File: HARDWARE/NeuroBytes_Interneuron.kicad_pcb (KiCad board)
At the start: 2 copper layers, 58.4 x 25.1 mm, 31 parts, among them P1 JST GH 4-POS, P2 JST GH 4-POS, P3 JST GH 4-POS, P4 JST GH 4-POS, P5 JST GH 4-POS, P6 JST GH 4-POS, P7 JST GH 4-POS, P8 JST_GH_5-pos, Q1 MMBT3904, Q2 MMBT3904, Q3 MMBT3904, SW1 SW_PUSH_TL3330AF130QG, U1 STM32L011Gx, U2 TLV702

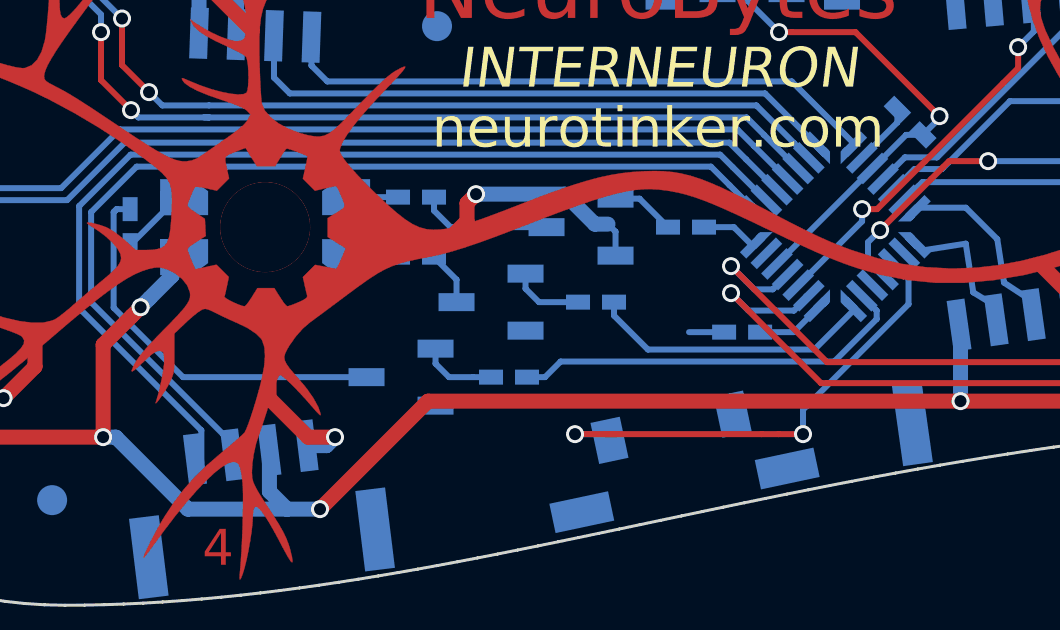
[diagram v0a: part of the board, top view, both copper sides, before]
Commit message: added ESD protection. updated title block.
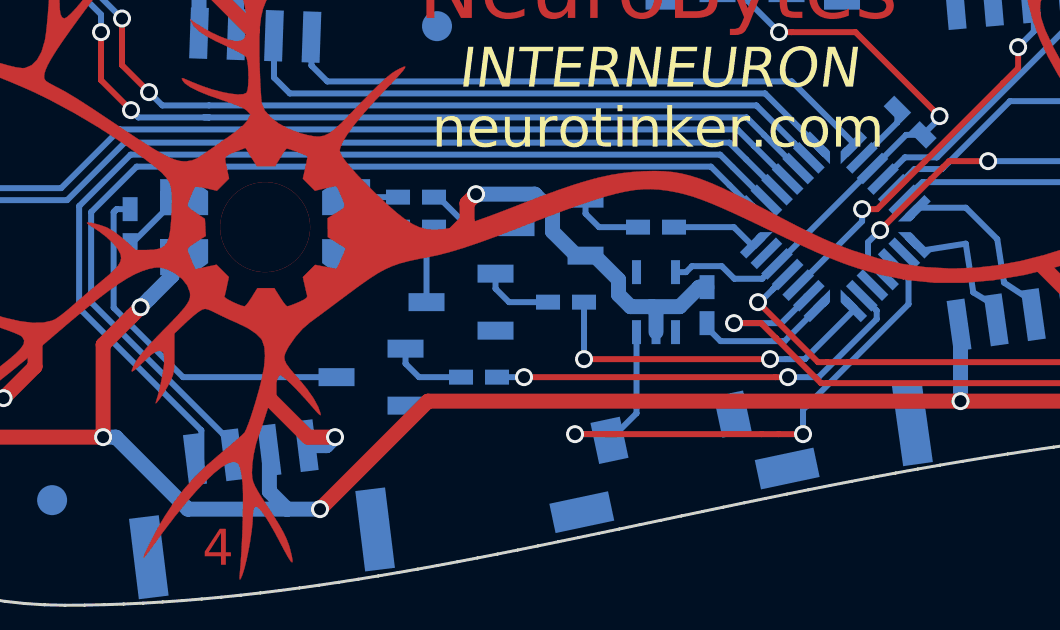
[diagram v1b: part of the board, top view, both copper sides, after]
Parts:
- added U3: RClamp0503F, KiCad_Footprints:ZF_SMD_SOT-353, B.Cu at (163.0, 92.5)
- moved R4 1.48 mm to (164.7, 92.6), turned to 90 degrees
- moved Q1 1.00 mm to (156.5, 92.5)
- moved Q2 1.00 mm to (159.5, 90.0)
- moved Q3 1.00 mm to (153.5, 95.0)
- moved R1 1.00 mm to (155.0, 90.0)
- moved R5 1.00 mm to (160.0, 92.5)
- moved R6 1.00 mm to (163.0, 90.0)
- moved R7 1.00 mm to (157.1, 95.0)
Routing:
- net SWITCH: track 16.3 -> 20.3 mm
- net GND: track 51.1 -> 55.1 mm
- net +3V3: track 22.8 -> 26.6 mm
- net LED_R: track 9.49 -> 11.7 mm, vias 0 -> 2
- net Net-(R4-Pad1): track 2.87 -> 4.71 mm
- net RESET: track 21.4 -> 19.7 mm
- net Net-(Q2-Pad3): track 4.43 -> 3.16 mm
- net Net-(Q3-Pad3): track 13.3 -> 12.3 mm
- net LED_B: track 13.4 -> 14.4 mm, vias 0 -> 2
- net LED_G: track 1.88 -> 2.68 mm
- net Net-(Q1-Pad3): track 1.81 -> 2.60 mm
- net A3EX: track 24.9 -> 24.2 mm

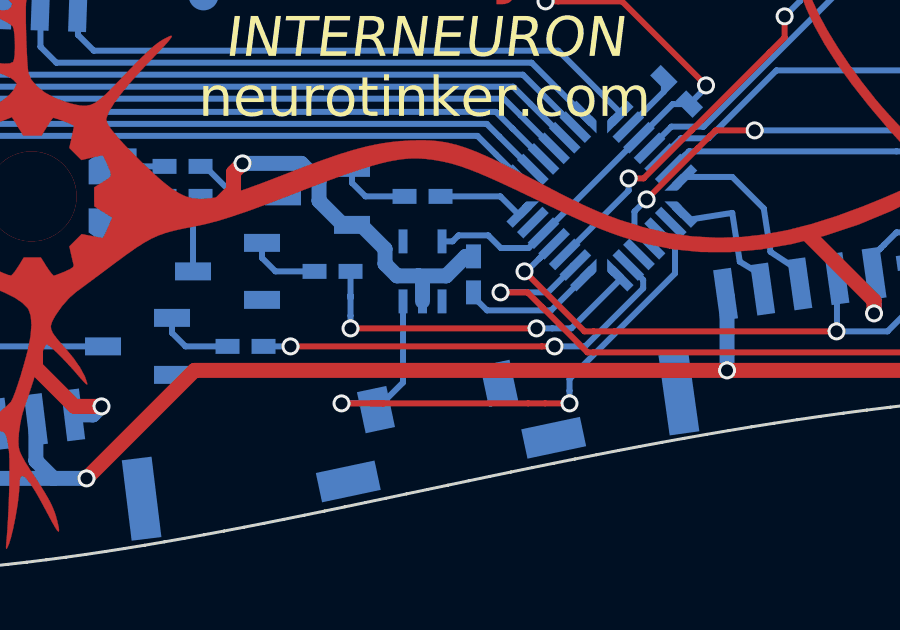
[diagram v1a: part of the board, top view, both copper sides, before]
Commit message: removed ESD protection (not needed during testing). generated fab files and BOM.
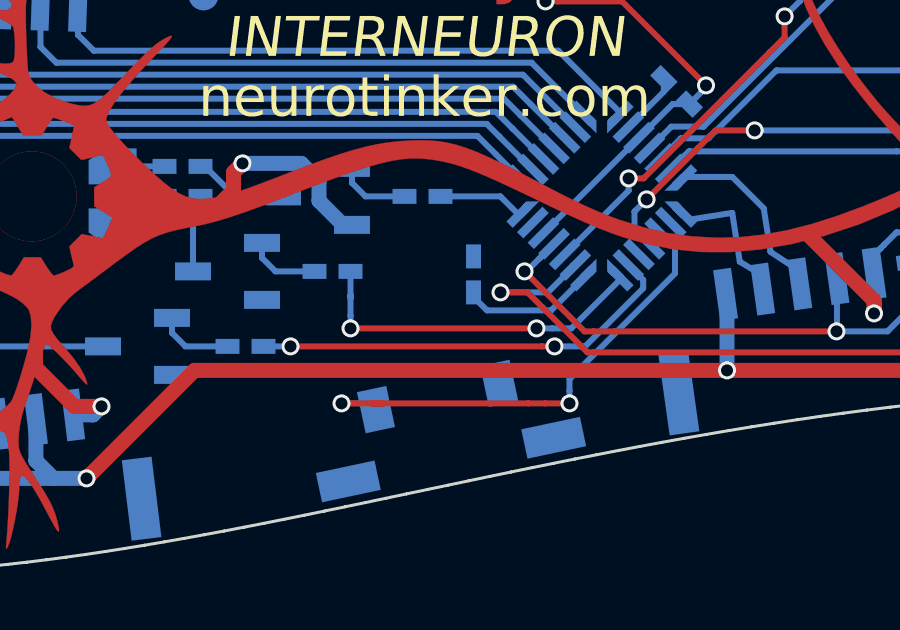
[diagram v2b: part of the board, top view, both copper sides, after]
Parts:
- removed U3: RClamp0503F, KiCad_Footprints:ZF_SMD_SOT-353
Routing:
- net GND: track 55.1 -> 49.2 mm
- net SWITCH: track 20.3 -> 16.3 mm
- net +3V3: track 26.6 -> 22.8 mm
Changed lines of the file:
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@@
     (links 104)
     (no_connects 0)
-    (area 130.957187 77.474012 189.496654 102.653506)
+    (area 123.4 55.4 221.257146 138.425)
     (thickness 1.6)
     (drawings 257)
-    (tracks 444)
+    (tracks 427)
     (zones 0)
-    (modules 32)
-    (nets 41)
+    (modules 31)
+    (nets 39)
   )
   (page A)
@@
       (drillshape 0)
       (scaleselection 1)
-      (outputdirectory ../../../NeuroTinker_RFQ_Sept2017/NeuroBytes_Interneuron/))
+      (outputdirectory ""))
   )
   (net 0 "")
@@
   (net 37 "Net-(U1-Pad23)")
   (net 38 "Net-(U1-Pad26)")
-  (net 39 "Net-(U3-Pad1)")
-  (net 40 "Net-(U3-Pad4)")
   (net_class Default "This is the default net class."
     (clearance 0.2)
@@
       (net 1 +5V))
   )
-  (module KiCad_Footprints:ZF_SMD_SOT-353 (layer B.Cu)
-    (at 163.03 92.5 180)
-    (fp_text reference U3 (at 0 -7.3 180) (layer B.SilkS) hide
-      (effects (font (size 1 1) (thickness 0.15)) (justify mirror))
-    )
-    (fp_text value RClamp0503F (at 0 4 180) (layer B.Fab) hide
-      (effects (font (size 1 1) (thickness 0.15)) (justify mirror))
-    )
-    (fp_circle (center -1.2 -0.8) (end -1.2 -0.6) (layer B.SilkS) (width 0.1))
-    (fp_line (start -1 0.6) (end 1 0.6) (layer B.SilkS) (width 0.1))
-    (fp_line (start -1 -0.6) (end -1 0.6) (layer B.SilkS) (width 0.1))
-    (fp_line (start 1 -0.6) (end -1 -0.6) (layer B.SilkS) (width 0.1))
-    (fp_line (start 1 0.6) (end 1 -0.6) (layer B.SilkS) (width 0.1))
-    (pad 1 smd rect (at -0.65 -1 180) (size 0.3 0.8) (layers B.Cu B.Paste B.Mask)
-      (net 39 "Net-(U3-Pad1)"))
-    (pad 2 smd rect (at 0 -1 180) (size 0.3 0.8) (layers B.Cu B.Paste B.Mask)
-      (net 2 GND))
-    (pad 3 smd rect (at 0.65 -1 180) (size 0.3 0.8) (layers B.Cu B.Paste B.Mask)
-      (net 22 SWITCH))
-    (pad 4 smd rect (at 0.65 1 180) (size 0.3 0.8) (layers B.Cu B.Paste B.Mask)
-      (net 40 "Net-(U3-Pad4)"))
-    (pad 5 smd rect (at -0.65 1 180) (size 0.3 0.8) (layers B.Cu B.Paste B.Mask)
-      (net 3 +3V3))
-  )
   (gr_line (start 125 90) (end 202 90) (layer Cmts.User) (width 0.2))
   (gr_line (start 128.53 102.5) (end 133.53 102.5) (layer F.Fab) (width 0.2))
@@
   (segment (start 182.532753 83.583364) (end 181.861002 84.255115) (width 0.5) (layer B.Cu) (net 1))
   (segment (start 183.027745 83.583364) (end 182.532753 83.583364) (width 0.5) (layer B.Cu) (net 1))
-  (segment (start 162.890001 92.649999) (end 163.819999 92.649999) (width 0.5) (layer B.Cu) (net 2))
-  (segment (start 163.819999 92.649999) (end 164.469998 92) (width 0.5) (layer B.Cu) (net 2))
-  (segment (start 164.469998 92) (end 164.73 92) (width 0.5) (layer B.Cu) (net 2))
   (segment (start 160.68 90.95) (end 160.98 90.95) (width 0.5) (layer B.Cu) (net 2))
-  (segment (start 160.98 90.95) (end 161.78 91.75) (width 0.5) (layer B.Cu) (net 2))
-  (segment (start 161.78 91.75) (end 161.78 92.25) (width 0.5) (layer B.Cu) (net 2))
-  (segment (start 161.78 92.25) (end 162.179999 92.649999) (width 0.5) (layer B.Cu) (net 2))
-  (segment (start 162.179999 92.649999) (end 162.890001 92.649999) (width 0.5) (layer B.Cu) (net 2))
-  (segment (start 162.890001 92.649999) (end 163.03 92.789998) (width 0.5) (layer B.Cu) (net 2))
-  (segment (start 163.03 92.789998) (end 163.03 93.5) (width 0.5) (layer B.Cu) (net 2))
   (segment (start 157.03 88.9) (end 158.990002 88.9) (width 0.5) (layer B.Cu) (net 2))
   (segment (start 158.990002 88.9) (end 159.58 89.489998) (width 0.5) (layer B.Cu) (net 2))
@@
   (segment (start 171.075736 86.51005) (end 171.075736 86.075736) (width 0.2) (layer B.Cu) (net 2))
   (segment (start 169.883883 87.701903) (end 171.075736 86.51005) (width 0.2) (layer B.Cu) (net 2))
-  (segment (start 165.220002 91.3) (end 164.23 91.3) (width 0.2) (layer B.Cu) (net 3))
-  (segment (start 164.23 91.3) (end 164.03 91.5) (width 0.2) (layer B.Cu) (net 3))
-  (segment (start 164.03 91.5) (end 163.68 91.5) (width 0.2) (layer B.Cu) (net 3))
-  (segment (start 167.062469 91.225804) (end 166.567495 91.720778) (width 0.2) (layer B.Cu) (net 3))
-  (segment (start 166.567495 91.720778) (end 165.64078 91.720778) (width 0.2) (layer B.Cu) (net 3))
-  (segment (start 165.64078 91.720778) (end 165.220002 91.3) (width 0.2) (layer B.Cu) (net 3))
   (segment (start 172.48 86.3) (end 172.48 86.368528) (width 0.2) (layer B.Cu) (net 3))
   (segment (start 172.48 86.368528) (end 171.924264 86.924264) (width 0.2) (layer B.Cu) (net 3))
@@
   (segment (start 165.624534 90) (end 163.830008 90) (width 0.2) (layer B.Cu) (net 21))
   (segment (start 165.624534 90) (end 166.249297 90.624763) (width 0.2) (layer B.Cu) (net 21))
-  (segment (start 161.478374 97.107374) (end 162.38 96.205748) (width 0.2) (layer B.Cu) (net 22))
-  (segment (start 162.38 96.205748) (end 162.38 93.5) (width 0.2) (layer B.Cu) (net 22))
   (segment (start 167.93 96.9) (end 167.93 96.475736) (width 0.2) (layer B.Cu) (net 22))
   (segment (start 167.93 96.475736) (end 167.93 96.085868) (width 0.2) (layer B.Cu) (net 22))
